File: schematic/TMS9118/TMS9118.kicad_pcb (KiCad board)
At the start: 2 copper layers, 87.1 x 66 mm, 31 parts, among them CON1 PICERINO-EDGE, J1 Conn_Coaxial, J10 Conn_01x03, J2 Conn_01x02, J3 Conn_01x02, J8 Conn_01x08, J9 Conn_01x08, U1 TMS4416, U14 TMS9118NL, U3 TMS4416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

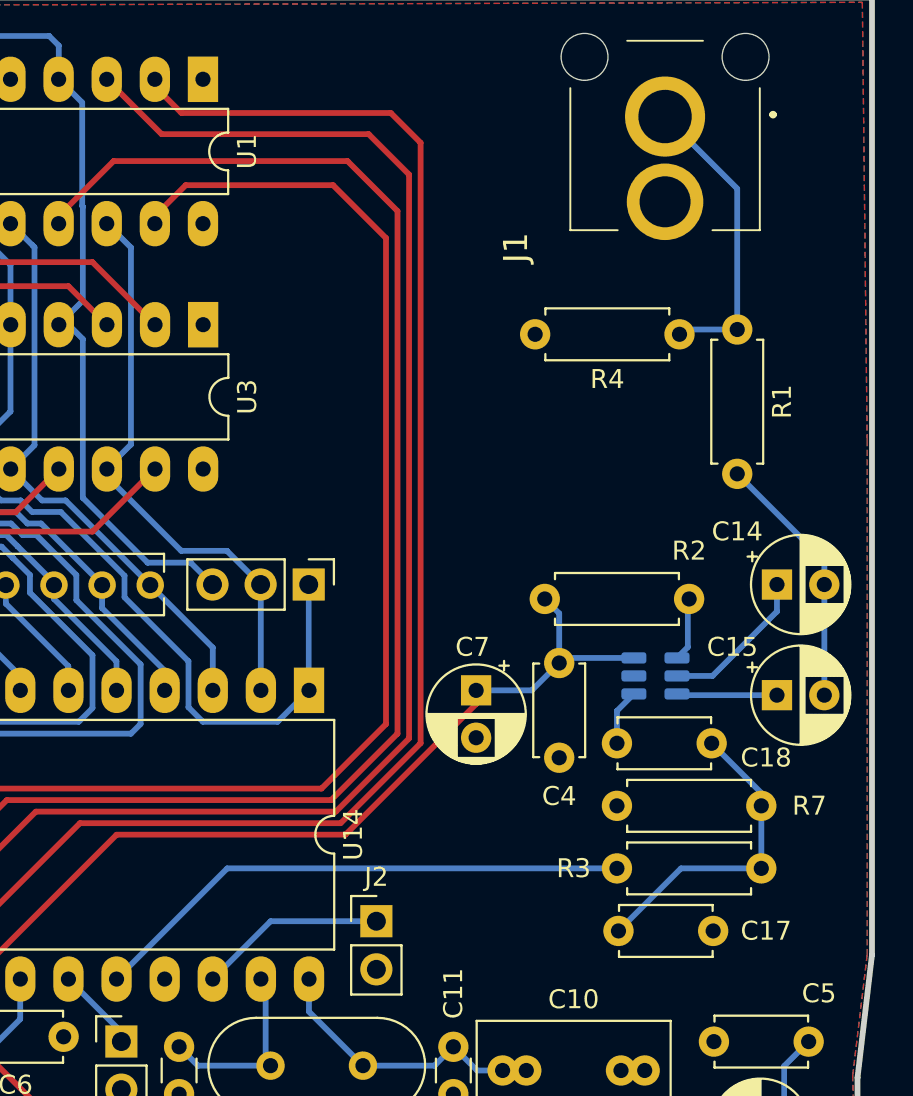
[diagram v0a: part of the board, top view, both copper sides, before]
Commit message: added new switch and sample video chip to simplify video output. work in progress.
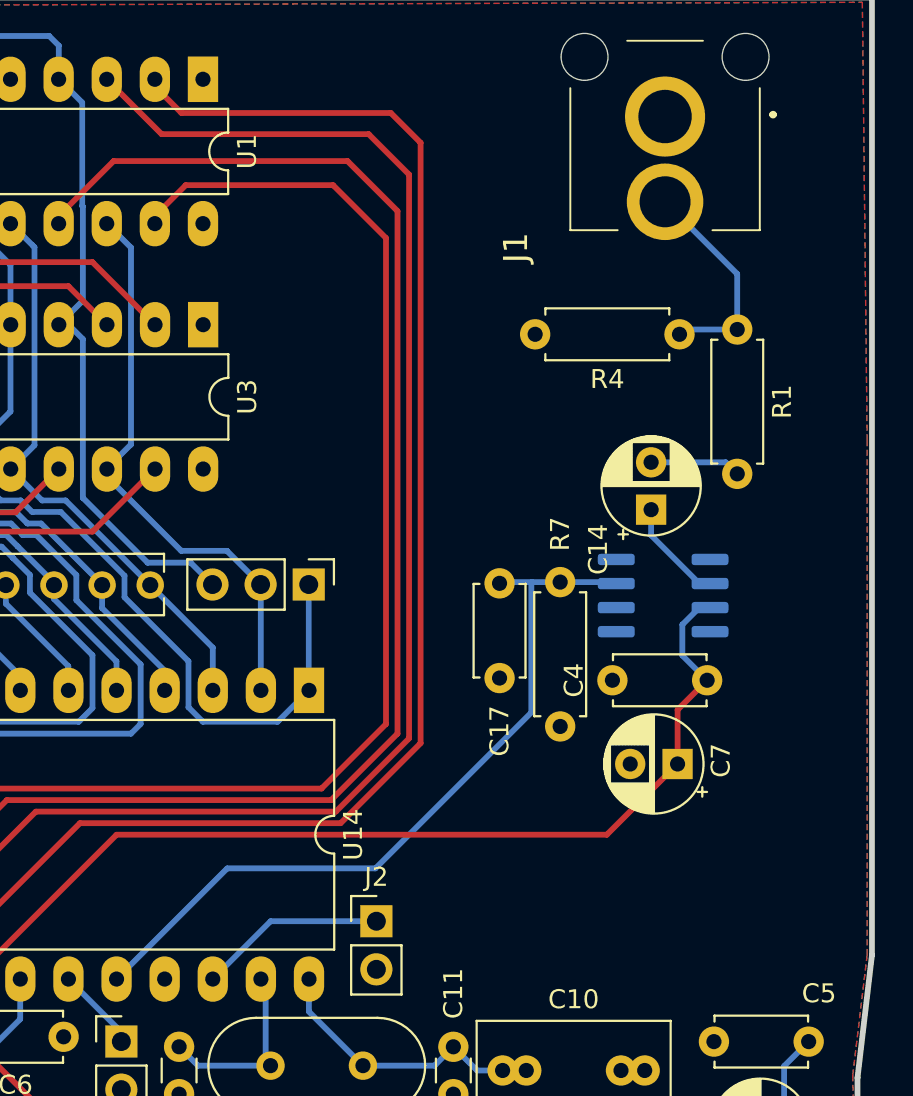
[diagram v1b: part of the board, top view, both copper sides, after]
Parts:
- removed C15: 33uF, Capacitor_THT:CP_Radial_D5.0mm_P2.50mm
- removed C18: 100nF, Capacitor_THT:C_Disc_D4.7mm_W2.5mm_P5.00mm
- removed R2: 10K, Resistor_THT:R_Axial_DIN0207_L6.3mm_D2.5mm_P7.62mm_Horizontal
- removed R3: 75R, Resistor_THT:R_Axial_DIN0207_L6.3mm_D2.5mm_P7.62mm_Horizontal
- removed U5: NJM2561, Package_TO_SOT_SMD:TSOT-23-6
- added U2: OPA832ID, Package_SO:SOIC-8_3.9x4.9mm_P1.27mm, B.Cu at (185.6, 111.6)
- C14: value 33uF -> 330uF
- moved C17 19.4 mm to (176.9, 110.9), turned to -90 degrees
- moved R7 15.9 mm to (180.1, 110.9), turned to -90 degrees
- moved C7 11.3 mm to (186.3, 120.5), turned to 180 degrees
- moved C4 7.86 mm to (187.9, 116.1), turned to 180 degrees
- moved C14 7.73 mm to (184.9, 107.0), turned to 90 degrees
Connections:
- C17 pad 1: Net-(C17-Pad1) -> /Y
- R7 pad 1: Net-(C17-Pad1) -> /Y
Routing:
- net Net-(C17-Pad1): track 16.6 -> 0.00 mm
- net /Y: track 28.8 -> 40.8 mm
- net Net-(C14-Pad2): track 13.6 -> 4.80 mm
- net VCC: track 183.5 -> 189.8 mm
- net Net-(U5-Vsag): track 5.30 -> 0.00 mm
- net Net-(J1-In): track 16.0 -> 11.5 mm
- net Net-(U5-PSave): track 3.38 -> 0.00 mm
- net Net-(U5-Vin): track 2.98 -> 0.00 mm
- net Net-(C14-Pad1): track 8.11 -> 5.59 mm

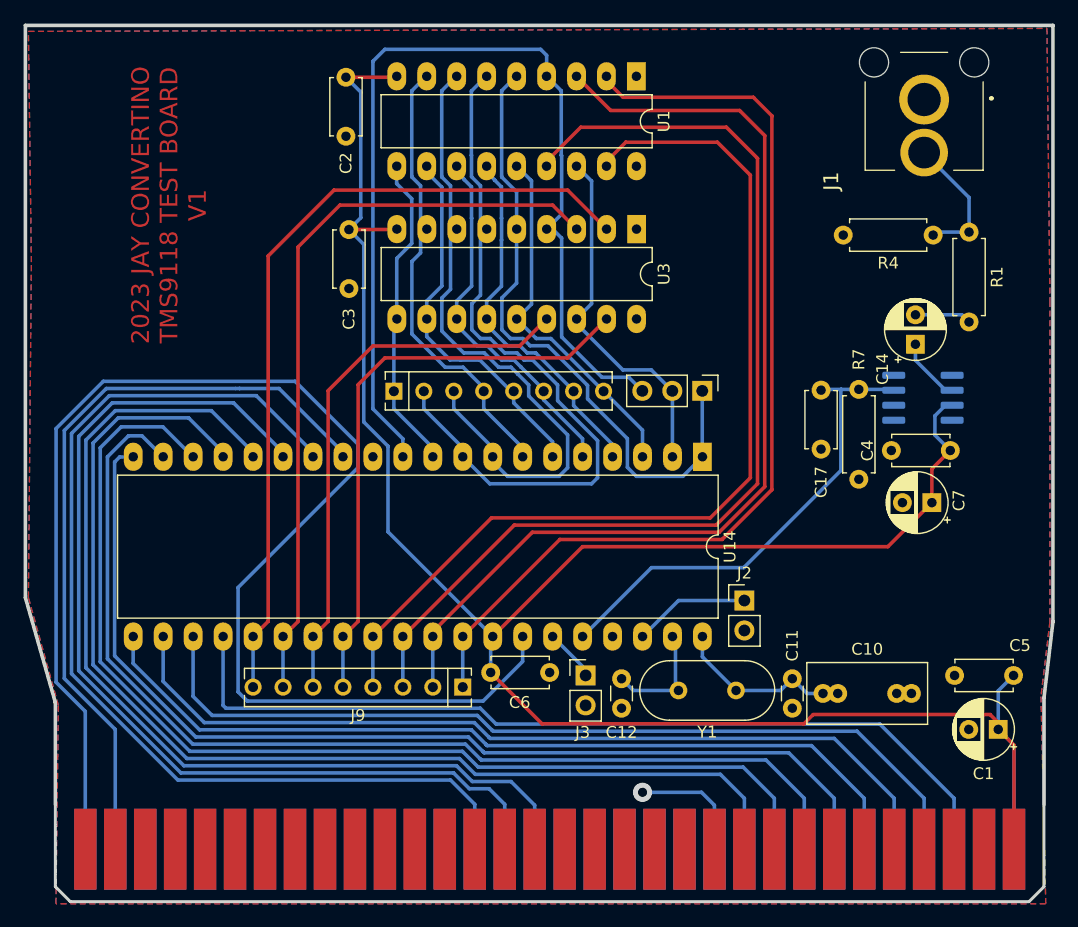
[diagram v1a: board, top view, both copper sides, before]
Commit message: initial commit of v2 tms992X board
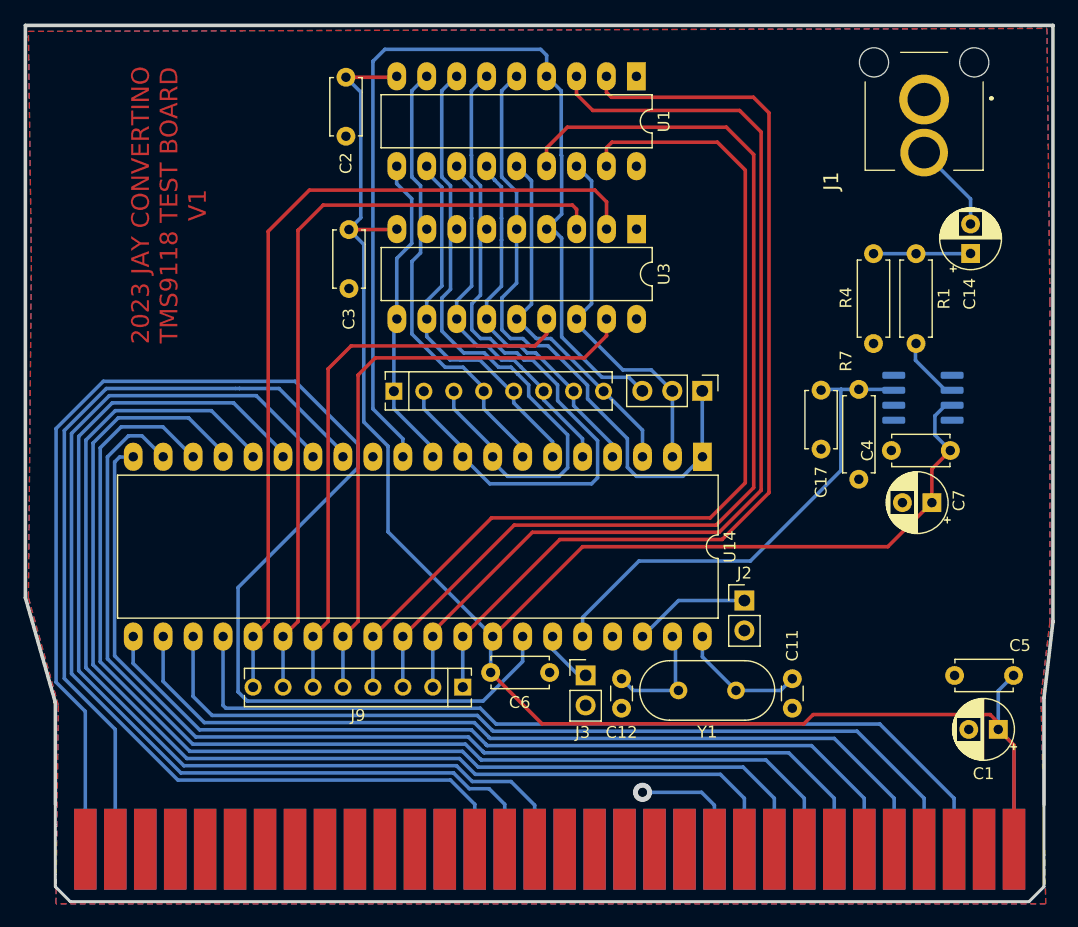
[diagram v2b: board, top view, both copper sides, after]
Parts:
- removed C10: 20pf, Capacitor_THT:C_Rect_L10.0mm_W5.0mm_P5.00mm_P7.50mm
- C11: value 18pF -> 33pF
- moved C14 9.00 mm to (189.6, 99.4)
- moved R4 5.29 mm to (181.4, 99.4), turned to -90 degrees
- moved R1 4.85 mm to (185.0, 99.4)
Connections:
- C14 pad 2: Net-(C14-Pad2) -> Net-(J1-In)
- R1 pad 1: Net-(J1-In) -> Net-(C14-Pad1)
- R1 pad 2: Net-(C14-Pad2) -> Net-(R1-Pad2)
- R4 pad 1: Net-(J1-In) -> Net-(C14-Pad1)
- U2 pad 6: Net-(C14-Pad1) -> Net-(R1-Pad2)
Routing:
- net Net-(R1-Pad2): track 0.00 -> 5.59 mm
- net Net-(C14-Pad2): track 4.80 -> 0.00 mm
- net Net-(J1-In): track 11.5 -> 7.69 mm
- net Net-(U14-XTAL1): track 14.0 -> 10.9 mm
- net Net-(C14-Pad1): track 5.59 -> 8.24 mm
- net /R7: track 69.5 -> 72.0 mm
- net /R5: track 46.7 -> 48.5 mm
- net /R6: track 63.8 -> 65.6 mm
- net /R4: track 49.5 -> 50.9 mm
- net /Y: track 40.8 -> 41.8 mm
- net /R1: track 85.7 -> 86.4 mm

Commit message: fixed tms9118 video output, opa832 failed
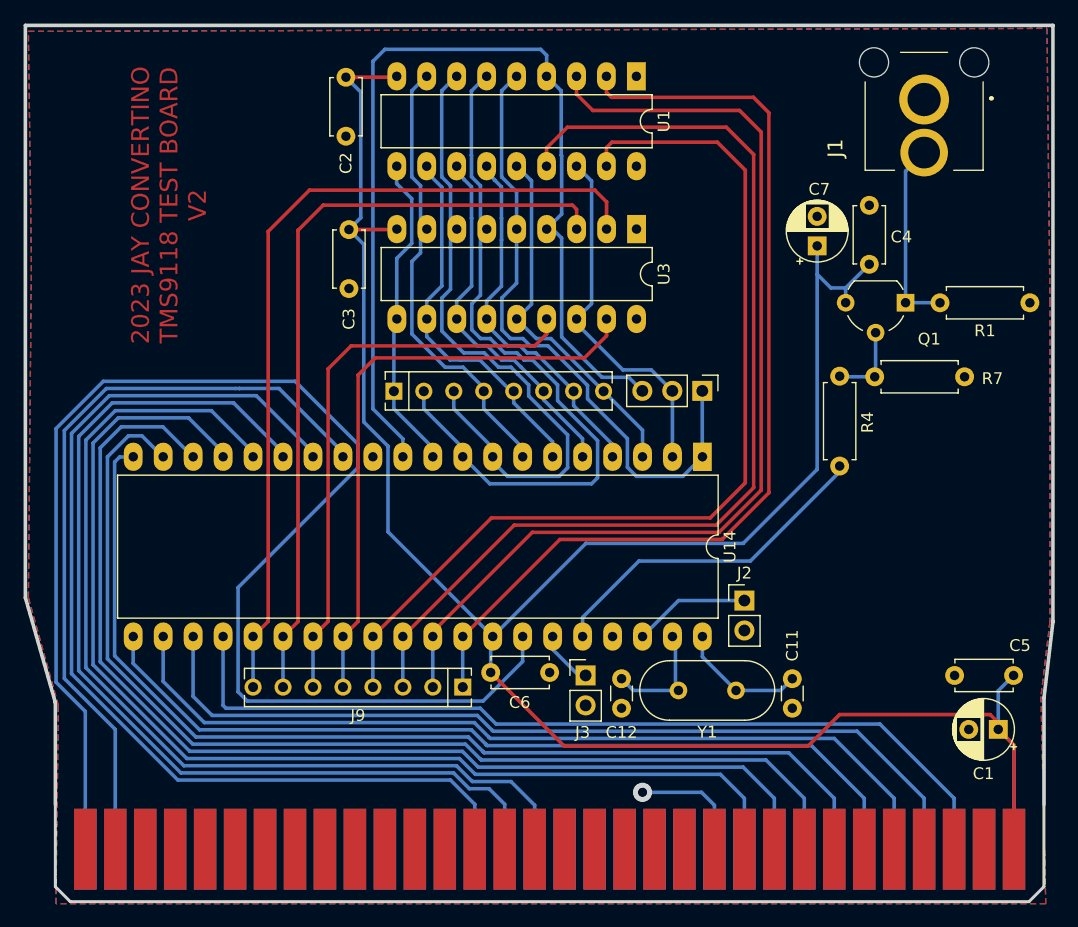
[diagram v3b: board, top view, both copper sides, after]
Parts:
- removed C14: 330uF, Capacitor_THT:CP_Radial_D5.0mm_P2.50mm
- removed C17: 220pf, Capacitor_THT:C_Disc_D4.7mm_W2.5mm_P5.00mm
- removed U2: OPA832ID, Package_SO:SOIC-8_3.9x4.9mm_P1.27mm
- added Q1: 2N3904, Package_TO_SOT_THT:TO-92_Wide, F.Cu at (184.1, 103.5)
- R4: value 75R -> 100R
- R7: value 470R -> 510R
- moved C7 23.8 mm to (176.6, 98.7), turned to 90 degrees
- moved C4 17.2 mm to (181.0, 100.3), turned to 90 degrees
- moved R4 10.8 mm to (178.5, 109.8)
- moved R1 10.5 mm to (194.6, 103.5), turned to 180 degrees
- moved R7 1.72 mm to (181.5, 109.8), turned to 0 degrees
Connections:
- R1 pad 1: Net-(C14-Pad1) -> VSS
- R1 pad 2: Net-(R1-Pad2) -> Net-(J1-In)
- R4 pad 1: Net-(C14-Pad1) -> Net-(Q1-B)
- R4 pad 2: VSS -> /Y
- R7 pad 1: /Y -> Net-(Q1-B)
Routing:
- net /Y: track 41.8 -> 28.8 mm
- net Net-(J1-In): track 7.69 -> 16.3 mm
- net VCC: track 189.8 -> 198.4 mm
- net Net-(C14-Pad1): track 8.24 -> 0.00 mm
- net Net-(Q1-B): track 0.00 -> 6.77 mm
- net Net-(R1-Pad2): track 5.59 -> 0.00 mm
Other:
- board text added: "2023 JAY CONVERTINO TMS9118 TEST BOARD V2"
- board text removed: "2023 JAY CONVERTINO TMS9118 TEST BOARD V1"
